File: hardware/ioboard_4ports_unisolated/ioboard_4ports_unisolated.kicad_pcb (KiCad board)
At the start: 2 copper layers, 106 x 55 mm, 54 parts, among them J1 Conn_02x06_Odd_Even, J10 XLR3, J11 XLR3, J12 Conn_01x03, J13 Conn_01x03, J2 XLR3, J3 XLR3, J4 XLR3, J5 XLR3, J6 Conn_01x03, J7 Conn_01x03, J8 XLR3, J9 XLR3, U1 M24C02-WMN, U2 SP3485EN, U3 SP3485EN, U4 SP3485EN, U5 SP3485EN

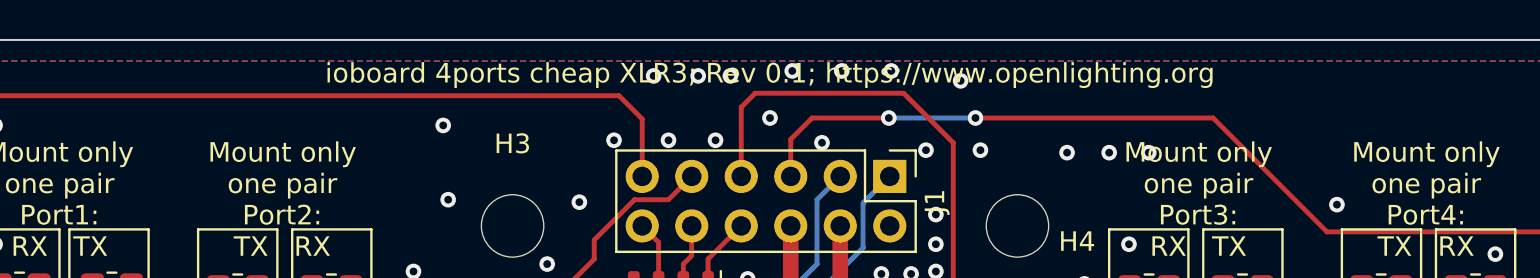
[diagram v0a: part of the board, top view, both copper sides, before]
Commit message: Unify board naming and bump all to rev 0.2
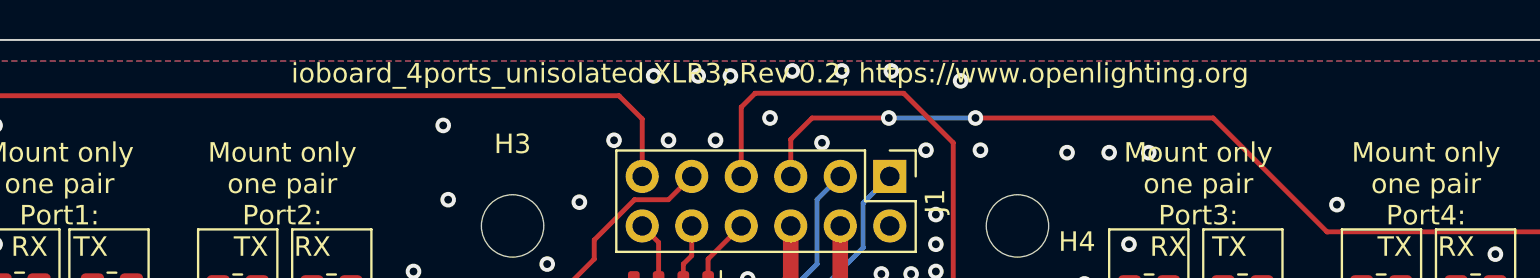
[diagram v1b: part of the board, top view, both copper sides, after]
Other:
- board text added: "ioboard_4ports_unisolated XLR3; Rev 0.2; https://www.openlighting.org"
- board text removed: "ioboard 4ports cheap XLR3; Rev 0.1; https://www.openlighting.org"

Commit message: Hardware: Make the reference path to the library relative and save the files with the new kicad version
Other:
- net class Default removed

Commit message: Finish IO-Board updates
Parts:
- U1: value M24C02-WMN -> M24C64-RMN6TP
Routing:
- net GND: vias 231 -> 222
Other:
- board text added: "ioboard_4ports_unisolated XLR3; Rev 0.5; https://github.com/OpenLightingProject/rp2040-dmxsun"
- board text removed: "ioboard_4ports_unisolated XLR3; Rev 0.2; https://www.openlighting.org"

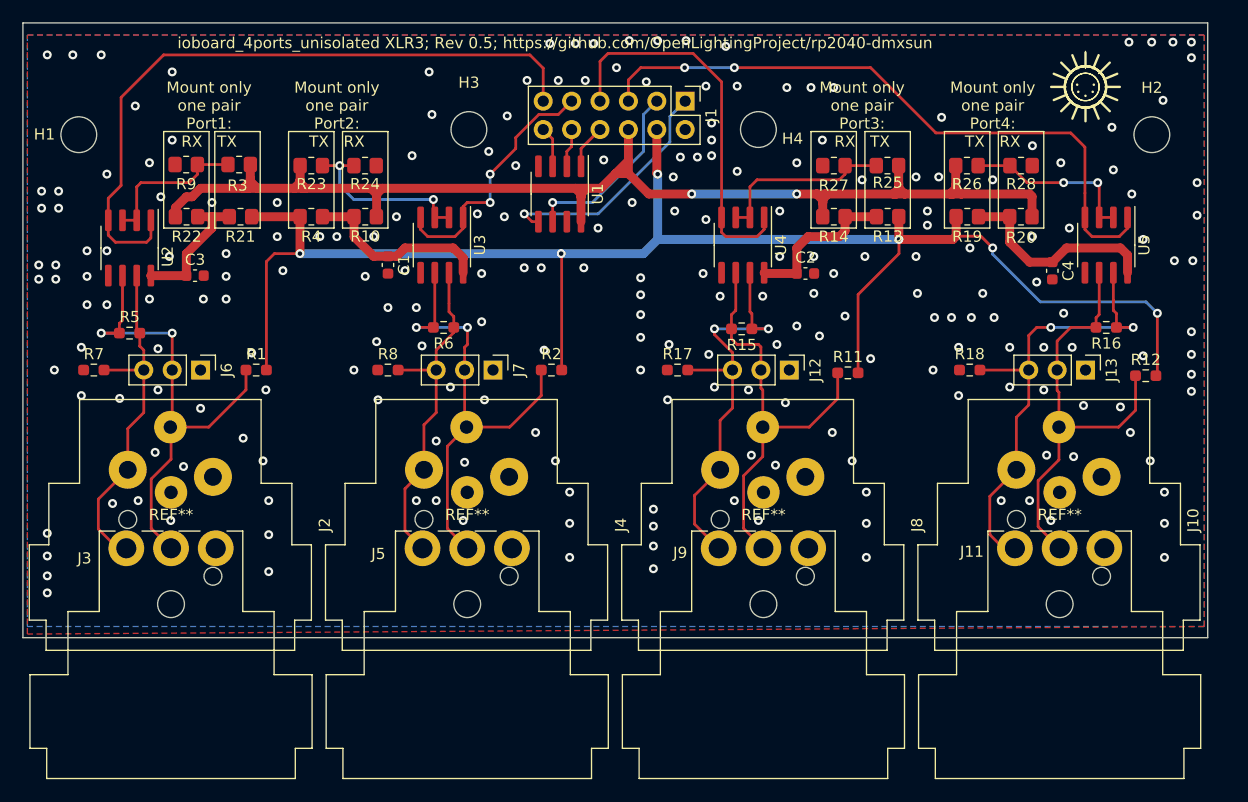
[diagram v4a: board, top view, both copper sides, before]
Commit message: Add RJ45 jack to ioboard_4ports_unisolated as well
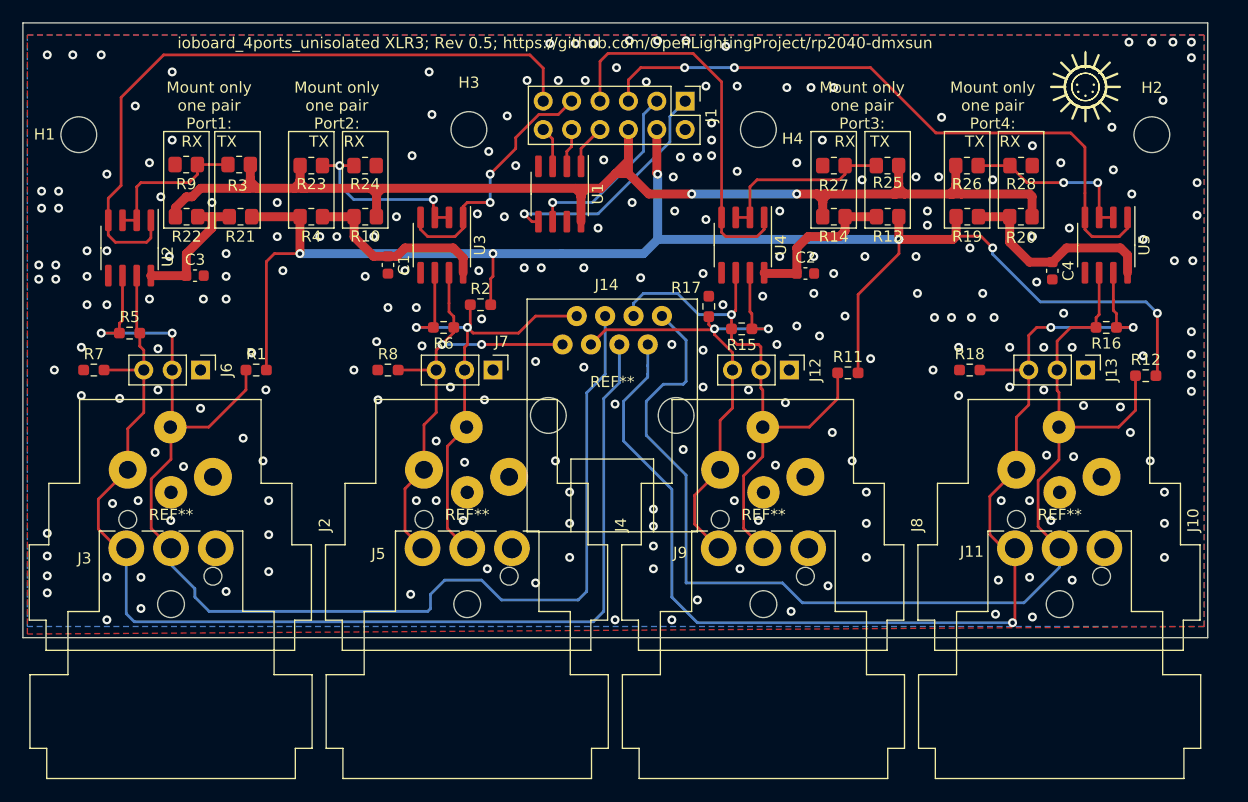
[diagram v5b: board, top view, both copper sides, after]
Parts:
- added J14: 8P8C, RJ45_Sparkfun:RJ45_Sparkfun, F.Cu at (77.7, 55.1)
- moved R2 8.63 mm to (65.9, 45.2)
- moved R17 6.34 mm to (86.4, 45.4), turned to -90 degrees
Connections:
- net Net-(J10-Pad2) renamed /RJ45_OUT_7
- net Net-(J10-Pad3) renamed /RJ45_OUT_8
- net Net-(J12-Pad2) renamed /RJ45_OUT_6
- net Net-(J12-Pad3) renamed /RJ45_OUT_5
- net Net-(J2-Pad2) renamed /RJ45_OUT_2
- net Net-(J2-Pad3) renamed /RJ45_OUT_1
- net Net-(J4-Pad2) renamed /RJ45_OUT_3
- net Net-(J4-Pad3) renamed /RJ45_OUT_4
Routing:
- net /RJ45_OUT_2: track 31.4 -> 105.1 mm
- net /RJ45_OUT_1: track 43.9 -> 113.0 mm
- net /RJ45_OUT_8: track 39.7 -> 105.7 mm
- net /RJ45_OUT_7: track 42.5 -> 106.0 mm, vias 2 -> 3
- net /RJ45_OUT_6: track 38.6 -> 49.6 mm, vias 0 -> 1
- net /RJ45_OUT_3: track 30.7 -> 41.5 mm, vias 0 -> 2
- net /RJ45_OUT_5: track 38.0 -> 47.0 mm
- net +5V: track 144.1 -> 138.3 mm
- net /RJ45_OUT_4: track 42.6 -> 45.2 mm
- net GND: vias 222 -> 238

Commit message: Bump all boards to rev 0.6
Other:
- board text added: "ioboard_4ports_unisolated XLR3; Rev 0.6; https://github.com/OpenLightingProject/rp2040-dmxsun"
- board text removed: "ioboard_4ports_unisolated XLR3; Rev 0.5; https://github.com/OpenLightingProject/rp2040-dmxsun"
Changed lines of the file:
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@@
     (effects (font (size 1 1) (thickness 0.15)))
   )
-  (gr_text "ioboard_4ports_unisolated XLR3; Rev 0.5; https://github.com/OpenLightingProject/rp2040-dmxsun" (at 72.6 21.8) (layer "F.SilkS")
+  (gr_text "ioboard_4ports_unisolated XLR3; Rev 0.6; https://github.com/OpenLightingProject/rp2040-dmxsun" (at 72.6 21.8) (layer "F.SilkS")
     (effects (font (size 1 1) (thickness 0.15)))
   )

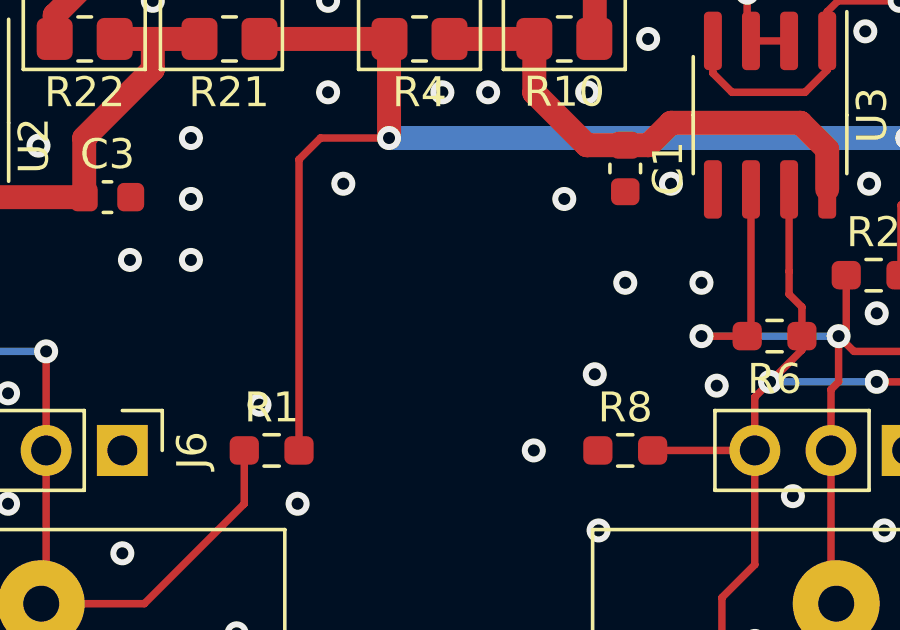
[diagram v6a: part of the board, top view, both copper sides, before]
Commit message: Update ioboards to KiCad 8, add OpenHardware logo
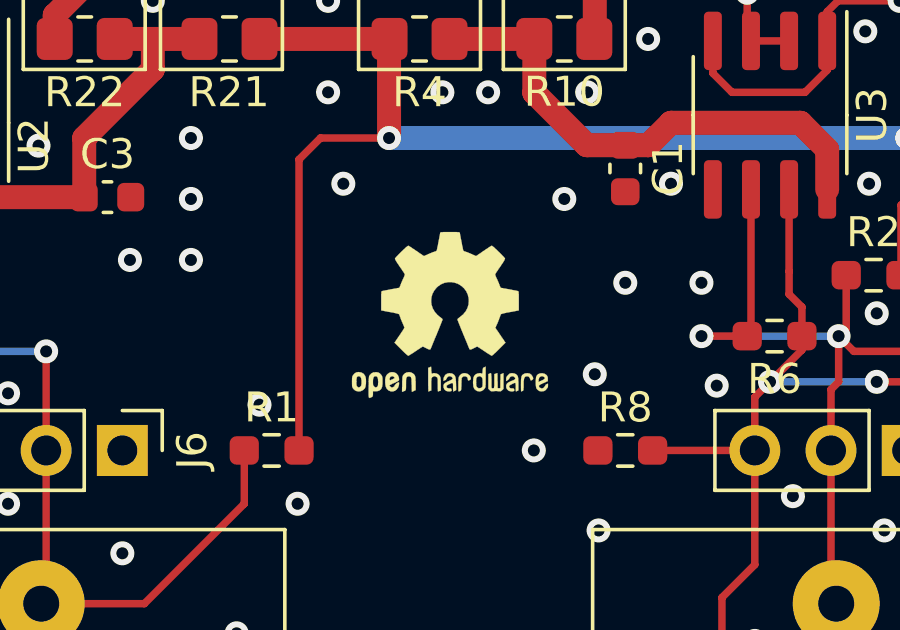
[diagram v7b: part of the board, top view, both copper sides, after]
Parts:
- added SYM1: Logo_Open_Hardware_Small, Symbol:OSHW-Logo2_7.3x6mm_SilkScreen, F.Cu at (51.8, 46.5)
